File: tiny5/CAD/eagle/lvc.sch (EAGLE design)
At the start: 35 parts, among them J1 3,5MM_1X2_SCREWTERM, J2 3,5MM_1X2_SCREWTERM, J3 2X3_50MIL, Q1 FDC6312P, Q2 PMGD280UN, Q3 DMP3010LPS, Q4 DMP3010LPS, U1 LT3007, U2 ATTINY5, U3 LT1494

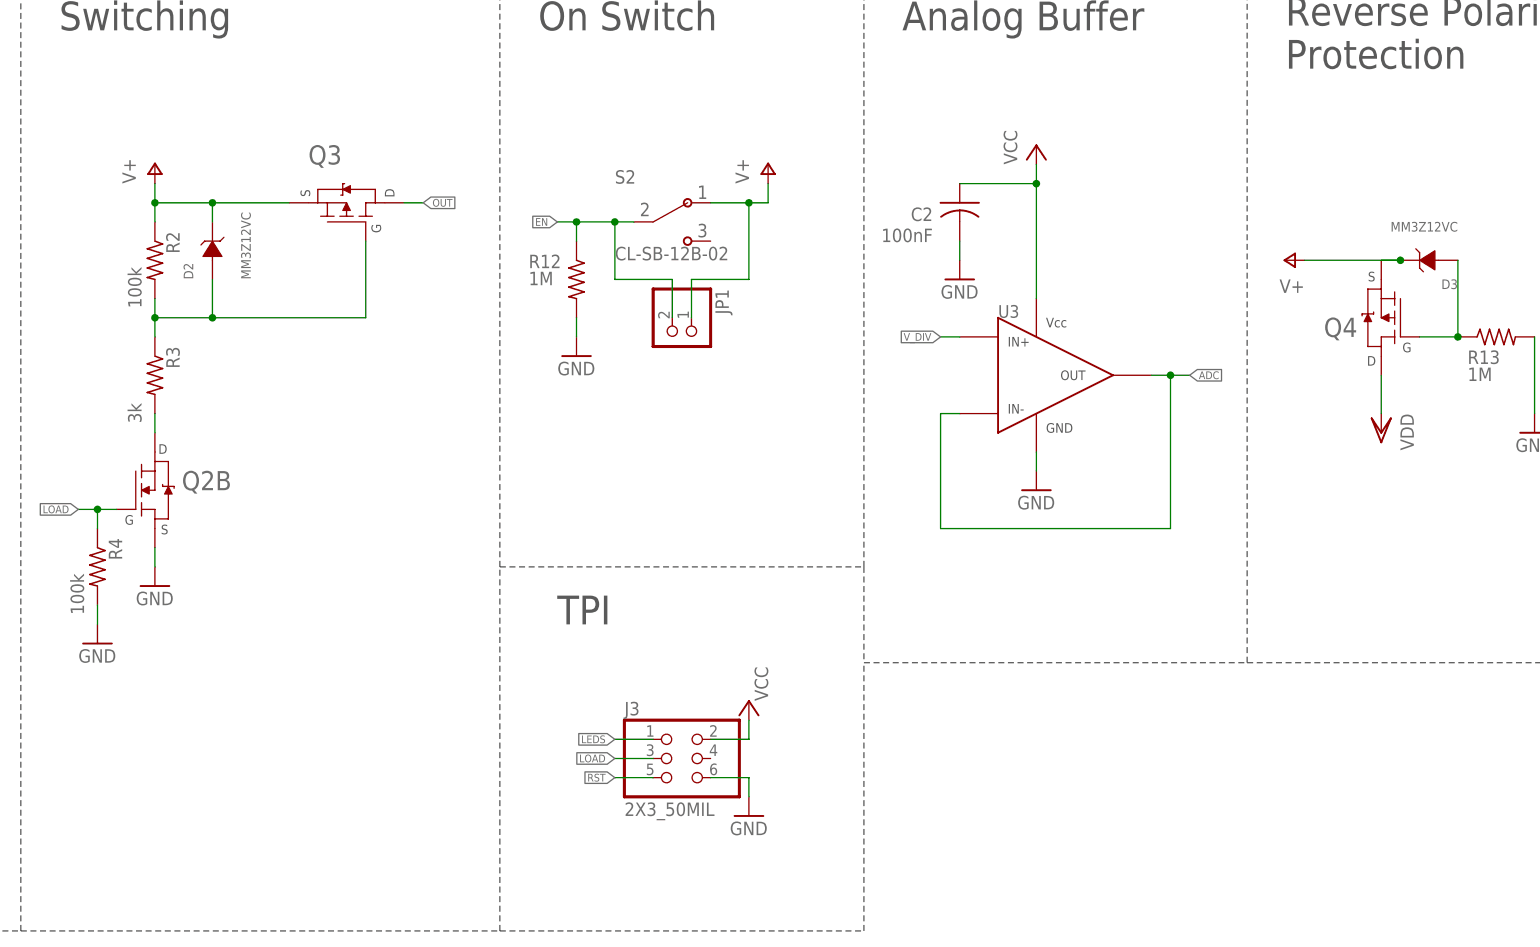
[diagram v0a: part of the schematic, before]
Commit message: yet another transistor (P-FET) update
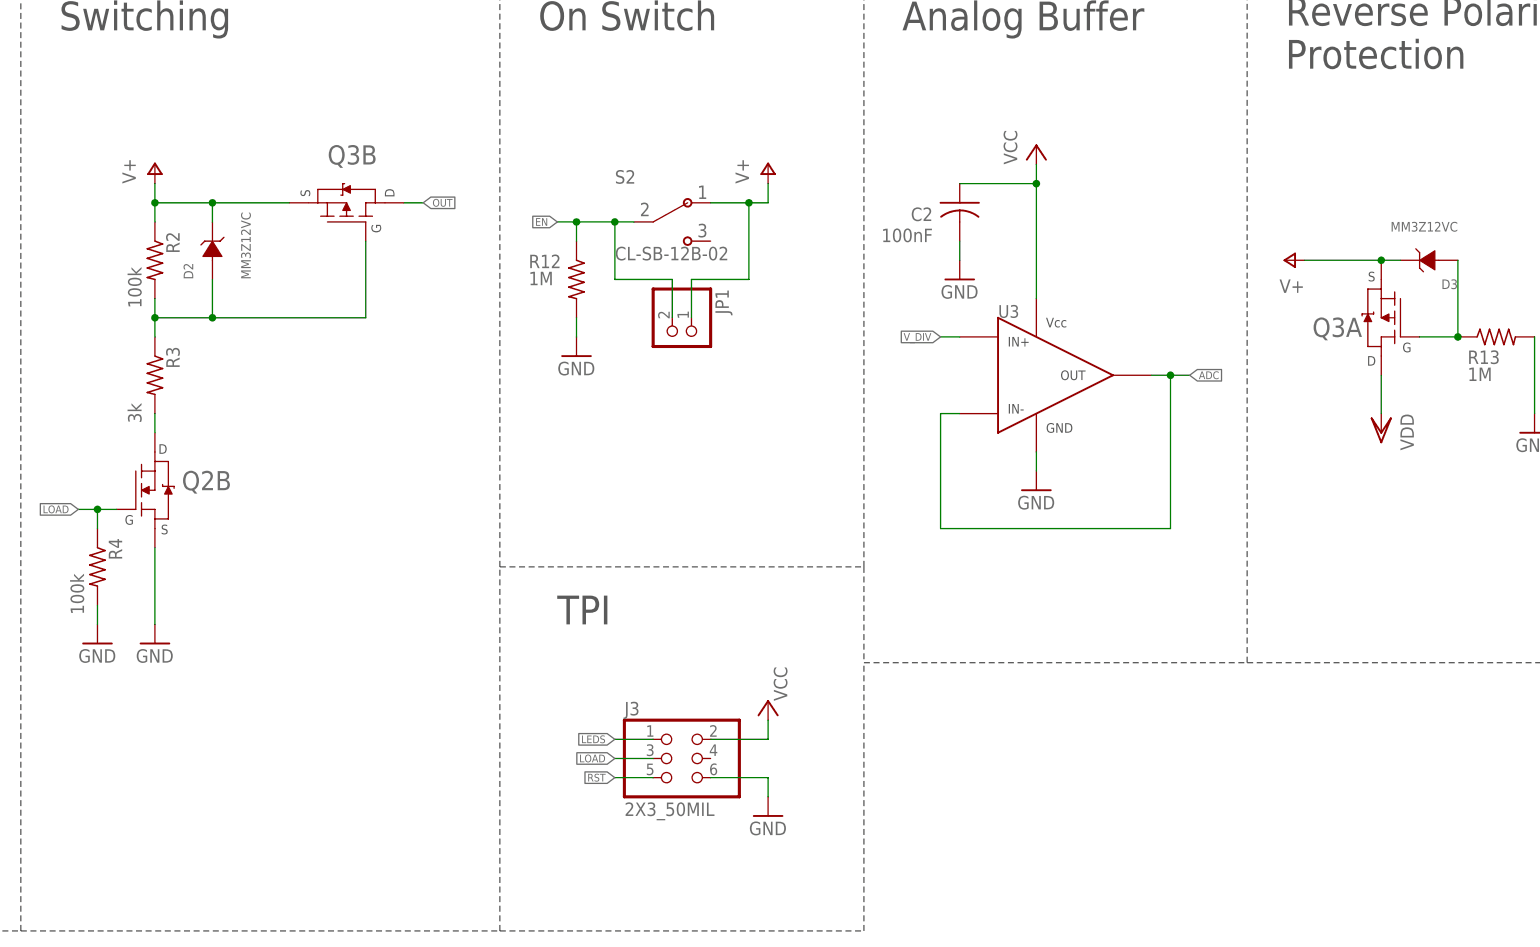
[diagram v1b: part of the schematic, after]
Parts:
- removed Q4: DMP3010LPS, AR_transistor:DMP3010LPS
- Q3: value DMP3010LPS -> SI7997DP; device AR_transistor:DMP3010LPS -> AR_transistor:SI7997DP
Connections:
- net N$5: now also Q3B.G; no longer Q3.G
- net N$6: now also Q3A.G; no longer Q4.G
- net OUT: now also Q3B.D; no longer Q3.D
- net V+: now also Q3A.S, Q3B.S; no longer Q3.S, Q4.S
- net VDD: now also Q3A.D; no longer Q4.D
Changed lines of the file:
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@@
 <part name="S2" library="AR_switches" deviceset="CL-SB-12B-02" device=""/>
 <part name="JP1" library="pinhead" deviceset="PINHD-1X2" device=""/>
-<part name="Q4" library="AR_transistor" deviceset="DMP3010LPS" device=""/>
 <part name="P+13" library="supply1" deviceset="V+" device=""/>
 <part name="VDD1" library="supply1" deviceset="VDD" device=""/>
@@
 <part name="R13" library="resistor" deviceset="R-US_" device="R0603" value="1M"/>
 <part name="GND19" library="supply1" deviceset="GND" device=""/>
-<part name="Q3" library="AR_transistor" deviceset="DMP3010LPS" device=""/>
+<part name="Q3" library="AR_transistor" deviceset="SI7997DP" device=""/>
 </parts>
 <sheets>
@@
 <instance part="D2" gate="G$1" x="83.82" y="96.52" rot="R90"/>
 <instance part="R3" gate="G$1" x="76.2" y="78.74" rot="R270"/>
-<instance part="GND7" gate="1" x="76.2" y="50.8"/>
+<instance part="GND7" gate="1" x="76.2" y="43.18"/>
 <instance part="GND8" gate="1" x="68.58" y="43.18"/>
 <instance part="R4" gate="G$1" x="68.58" y="53.34" rot="R270"/>
@@
 <instance part="TP1" gate="G$1" x="160.02" y="182.88"/>
 <instance part="J3" gate="G$1" x="147.32" y="27.94"/>
-<instance part="P+11" gate="VCC" x="154.94" y="35.56" smashed="yes">
-<attribute name="VALUE" x="157.48" y="35.56" size="1.778" layer="96" rot="R90"/>
-</instance>
-<instance part="GND17" gate="1" x="154.94" y="20.32"/>
+<instance part="P+11" gate="VCC" x="157.48" y="35.56" smashed="yes">
+<attribute name="VALUE" x="160.02" y="35.56" size="1.778" layer="96" rot="R90"/>
+</instance>
+<instance part="GND17" gate="1" x="157.48" y="20.32"/>
 <instance part="R12" gate="G$1" x="132.08" y="91.44" smashed="yes" rot="R270">
 <attribute name="NAME" x="125.73" y="92.9386" size="1.778" layer="95"/>
@@
 <instance part="S2" gate="G$1" x="144.78" y="99.06"/>
 <instance part="JP1" gate="G$1" x="144.78" y="83.82" rot="R270"/>
-<instance part="Q4" gate="G$1" x="238.76" y="86.36" smashed="yes">
-<attribute name="NAME" x="231.14" y="86.36" size="2.54" layer="95" rot="MR180"/>
-</instance>
 <instance part="P+13" gate="1" x="226.06" y="93.98" rot="R90"/>
 <instance part="VDD1" gate="G$1" x="251.46" y="157.48" rot="R270"/>
@@
 </instance>
 <instance part="GND19" gate="1" x="259.08" y="71.12"/>
-<instance part="Q3" gate="G$1" x="101.6" y="101.6" smashed="yes" rot="MR270">
-<attribute name="NAME" x="96.52" y="106.68" size="2.54" layer="95"/>
+<instance part="Q3" gate="B" x="101.6" y="101.6" smashed="yes" rot="MR270">
+<attribute name="NAME" x="99.06" y="106.68" size="2.54" layer="95"/>
+</instance>
+<instance part="Q3" gate="A" x="238.76" y="86.36" smashed="yes">
+<attribute name="NAME" x="236.22" y="83.82" size="2.54" layer="95" rot="MR0"/>
 </instance>
 </instances>
@@
 <pinref part="Q2" gate="B" pin="S"/>
 <pinref part="GND7" gate="1" pin="GND"/>
-<wire x1="76.2" y1="55.88" x2="76.2" y2="53.34" width="0.1524" layer="91"/>
+<wire x1="76.2" y1="55.88" x2="76.2" y2="45.72" width="0.1524" layer="91"/>
 </segment>
 <segment>
@@
 <segment>
 <pinref part="J3" gate="G$1" pin="6"/>
-<wire x1="149.86" y1="25.4" x2="154.94" y2="25.4" width="0.1524" layer="91"/>
-<wire x1="154.94" y1="25.4" x2="154.94" y2="22.86" width="0.1524" layer="91"/>
+<wire x1="149.86" y1="25.4" x2="157.48" y2="25.4" width="0.1524" layer="91"/>
+<wire x1="157.48" y1="25.4" x2="157.48" y2="22.86" width="0.1524" layer="91"/>
 <pinref part="GND17" gate="1" pin="GND"/>
 </segment>
@@
 <wire x1="83.82" y1="99.06" x2="83.82" y2="101.6" width="0.1524" layer="91"/>
 <junction x="83.82" y="101.6"/>
-<pinref part="Q3" gate="G$1" pin="S"/>
+<pinref part="Q3" gate="B" pin="S"/>
 </segment>
 <segment>
@@
 </segment>
 <segment>
-<pinref part="Q4" gate="G$1" pin="S"/>
 <pinref part="P+13" gate="1" pin="V+"/>
-<wire x1="228.6" y1="93.98" x2="241.3" y2="93.98" width="0.1524" layer="91"/>
+<wire x1="228.6" y1="93.98" x2="238.76" y2="93.98" width="0.1524" layer="91"/>
 <pinref part="D3" gate="G$1" pin="C"/>
-<junction x="241.3" y="93.98"/>
-<wire x1="241.3" y1="93.98" x2="238.76" y2="93.98" width="0.1524" layer="91"/>
+<pinref part="Q3" gate="A" pin="S"/>
+<wire x1="238.76" y1="93.98" x2="241.3" y2="93.98" width="0.1524" layer="91"/>
+<junction x="238.76" y="93.98"/>
 </segment>
 </net>
@@
 <pinref part="J3" gate="G$1" pin="2"/>
 <pinref part="P+11" gate="VCC" pin="VCC"/>
-<wire x1="149.86" y1="30.48" x2="154.94" y2="30.48" width="0.1524" layer="91"/>
-<wire x1="154.94" y1="30.48" x2="154.94" y2="33.02" width="0.1524" layer="91"/>
+<wire x1="149.86" y1="30.48" x2="157.48" y2="30.48" width="0.1524" layer="91"/>
+<wire x1="157.48" y1="30.48" x2="157.48" y2="33.02" width="0.1524" layer="91"/>
 </segment>
 </net>
@@
 <wire x1="76.2" y1="83.82" x2="76.2" y2="86.36" width="0.1524" layer="91"/>
 <junction x="76.2" y="86.36"/>
-<pinref part="Q3" gate="G$1" pin="G"/>
+<pinref part="Q3" gate="B" pin="G"/>
 </segment>
 </net>
@@
 <wire x1="109.22" y1="101.6" x2="111.76" y2="101.6" width="0.1524" layer="91"/>
 <label x="111.76" y="101.6" size="1.016" layer="95" xref="yes"/>
-<pinref part="Q3" gate="G$1" pin="D"/>
+<pinref part="Q3" gate="B" pin="D"/>
 </segment>
 <segment>
@@
 </segment>
 <segment>
-<pinref part="Q4" gate="G$1" pin="D"/>
 <pinref part="VDD2" gate="G$1" pin="VDD"/>
 <wire x1="238.76" y1="73.66" x2="238.76" y2="78.74" width="0.1524" layer="91"/>
+<pinref part="Q3" gate="A" pin="D"/>
 </segment>
 </net>
@@
 <pinref part="D3" gate="G$1" pin="A"/>
 <wire x1="248.92" y1="93.98" x2="248.92" y2="83.82" width="0.1524" layer="91"/>
-<pinref part="Q4" gate="G$1" pin="G"/>
 <wire x1="248.92" y1="83.82" x2="243.84" y2="83.82" width="0.1524" layer="91"/>
 <pinref part="R13" gate="G$1" pin="1"/>
 <junction x="248.92" y="83.82"/>
-</segment>
-</net>
+<pinref part="Q3" gate="A" pin="G"/>
+</segment>
+</net>

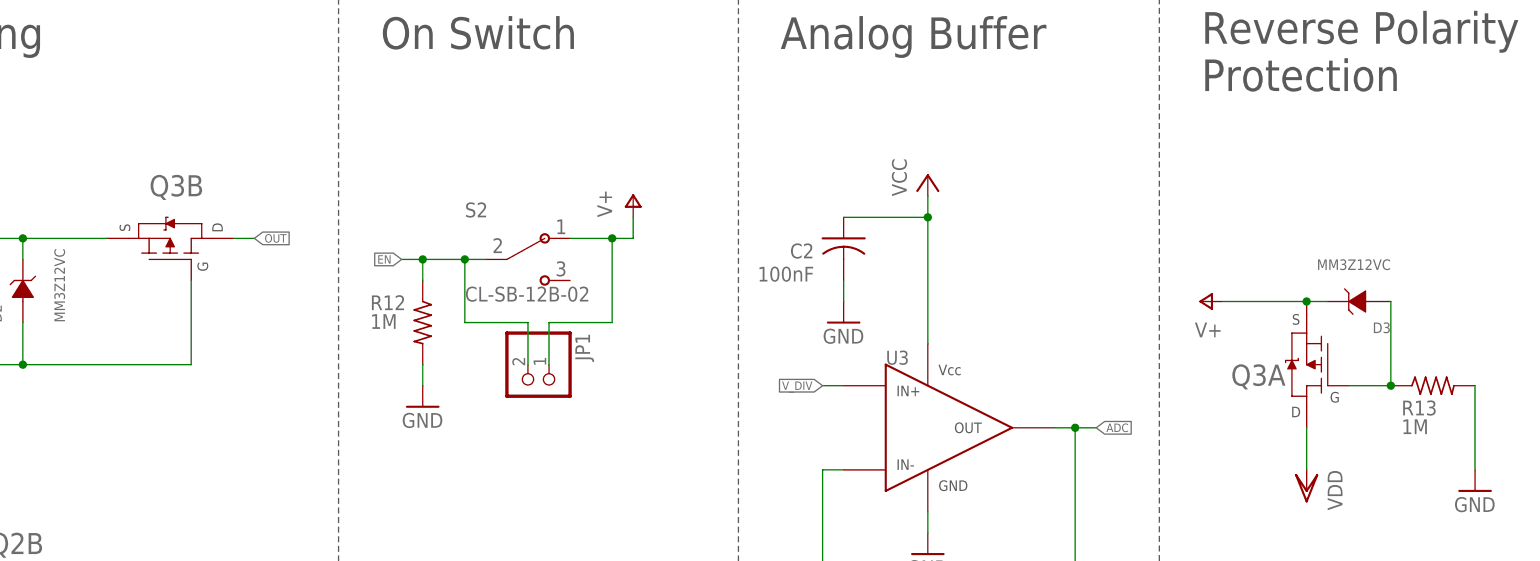
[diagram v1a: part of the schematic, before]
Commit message: Routed new transistor. Cleaned up transistor package definition
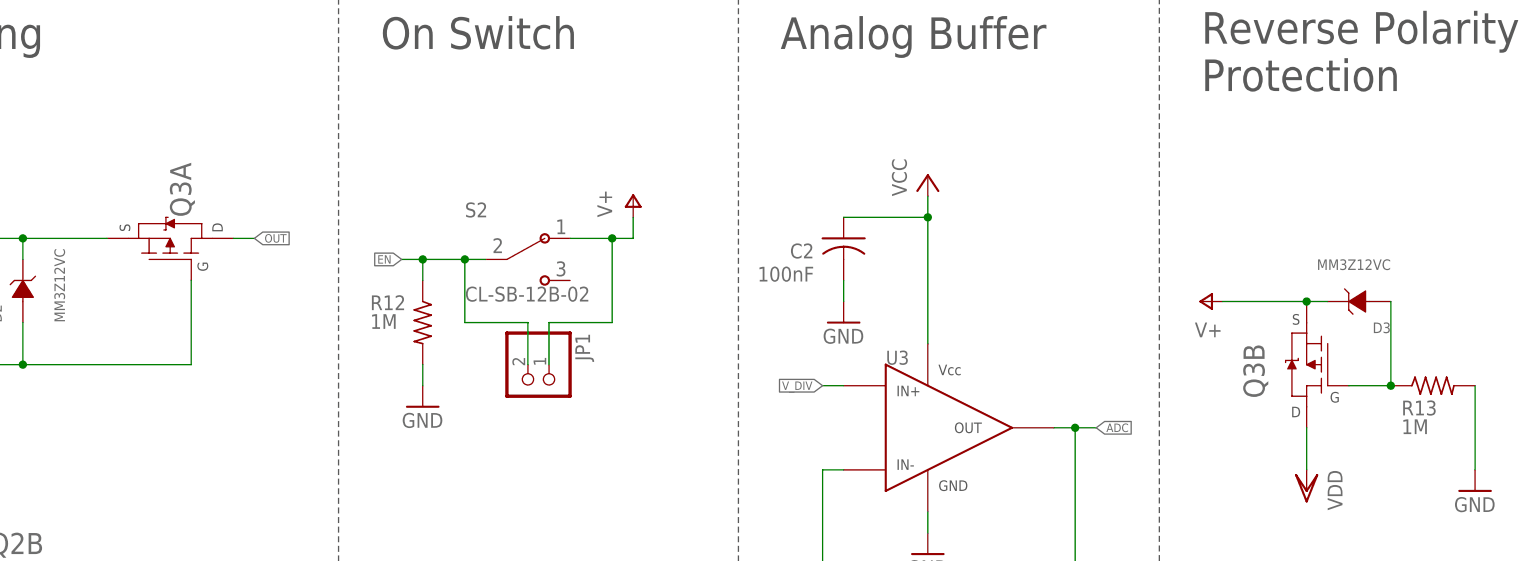
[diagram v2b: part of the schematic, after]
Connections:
- net N$5: now also Q3A.G; no longer Q3B.G
- net N$6: now also Q3B.G; no longer Q3A.G
- net OUT: now also Q3A.D; no longer Q3B.D
- net VDD: now also Q3B.D; no longer Q3A.D
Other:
- moved on the sheet: Q3A, Q3B
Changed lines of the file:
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@@
 <?xml version="1.0" encoding="utf-8"?>
 <!DOCTYPE eagle SYSTEM "eagle.dtd">
-<eagle version="7.6.0">
+<eagle version="6.5.0">
 <drawing>
 <settings>
@@
 </instance>
 <instance part="GND19" gate="1" x="259.08" y="71.12"/>
-<instance part="Q3" gate="B" x="101.6" y="101.6" smashed="yes" rot="MR270">
-<attribute name="NAME" x="99.06" y="106.68" size="2.54" layer="95"/>
-</instance>
-<instance part="Q3" gate="A" x="238.76" y="86.36" smashed="yes">
-<attribute name="NAME" x="236.22" y="83.82" size="2.54" layer="95" rot="MR0"/>
+<instance part="Q3" gate="B" x="238.76" y="86.36" smashed="yes">
+<attribute name="NAME" x="233.68" y="88.9" size="2.54" layer="95" rot="MR270"/>
+</instance>
+<instance part="Q3" gate="A" x="101.6" y="101.6" smashed="yes" rot="MR270">
+<attribute name="NAME" x="104.14" y="104.14" size="2.54" layer="95" rot="R90"/>
 </instance>
 </instances>
@@
 <segment>
 <pinref part="P+4" gate="1" pin="V+"/>
-<wire x1="93.98" y1="101.6" x2="83.82" y2="101.6" width="0.1524" layer="91"/>
 <wire x1="83.82" y1="101.6" x2="76.2" y2="101.6" width="0.1524" layer="91"/>
 <wire x1="76.2" y1="101.6" x2="76.2" y2="104.14" width="0.1524" layer="91"/>
@@
 <pinref part="D2" gate="G$1" pin="C"/>
 <wire x1="83.82" y1="99.06" x2="83.82" y2="101.6" width="0.1524" layer="91"/>
+<pinref part="Q3" gate="A" pin="S"/>
+<wire x1="93.98" y1="101.6" x2="83.82" y2="101.6" width="0.1524" layer="91"/>
 <junction x="83.82" y="101.6"/>
-<pinref part="Q3" gate="B" pin="S"/>
 </segment>
 <segment>
@@
 </segment>
 <segment>
+<pinref part="D3" gate="G$1" pin="C"/>
+<pinref part="Q3" gate="B" pin="S"/>
+<wire x1="241.3" y1="93.98" x2="238.76" y2="93.98" width="0.1524" layer="91"/>
 <pinref part="P+13" gate="1" pin="V+"/>
-<wire x1="228.6" y1="93.98" x2="238.76" y2="93.98" width="0.1524" layer="91"/>
-<pinref part="D3" gate="G$1" pin="C"/>
-<pinref part="Q3" gate="A" pin="S"/>
-<wire x1="238.76" y1="93.98" x2="241.3" y2="93.98" width="0.1524" layer="91"/>
+<wire x1="238.76" y1="93.98" x2="228.6" y2="93.98" width="0.1524" layer="91"/>
 <junction x="238.76" y="93.98"/>
 </segment>
@@
 <wire x1="76.2" y1="86.36" x2="83.82" y2="86.36" width="0.1524" layer="91"/>
 <wire x1="83.82" y1="86.36" x2="104.14" y2="86.36" width="0.1524" layer="91"/>
-<wire x1="104.14" y1="86.36" x2="104.14" y2="96.52" width="0.1524" layer="91"/>
 <pinref part="D2" gate="G$1" pin="A"/>
 <wire x1="83.82" y1="91.44" x2="83.82" y2="86.36" width="0.1524" layer="91"/>
@@
 <wire x1="76.2" y1="83.82" x2="76.2" y2="86.36" width="0.1524" layer="91"/>
 <junction x="76.2" y="86.36"/>
-<pinref part="Q3" gate="B" pin="G"/>
+<pinref part="Q3" gate="A" pin="G"/>
+<wire x1="104.14" y1="96.52" x2="104.14" y2="86.36" width="0.1524" layer="91"/>
 </segment>
 </net>
@@
 <net name="OUT" class="0">
 <segment>
-<wire x1="109.22" y1="101.6" x2="111.76" y2="101.6" width="0.1524" layer="91"/>
 <label x="111.76" y="101.6" size="1.016" layer="95" xref="yes"/>
-<pinref part="Q3" gate="B" pin="D"/>
+<pinref part="Q3" gate="A" pin="D"/>
+<wire x1="111.76" y1="101.6" x2="109.22" y2="101.6" width="0.1524" layer="91"/>
 </segment>
 <segment>
@@
 <segment>
 <pinref part="VDD2" gate="G$1" pin="VDD"/>
+<pinref part="Q3" gate="B" pin="D"/>
 <wire x1="238.76" y1="73.66" x2="238.76" y2="78.74" width="0.1524" layer="91"/>
-<pinref part="Q3" gate="A" pin="D"/>
 </segment>
 </net>
@@
 <pinref part="D3" gate="G$1" pin="A"/>
 <wire x1="248.92" y1="93.98" x2="248.92" y2="83.82" width="0.1524" layer="91"/>
-<wire x1="248.92" y1="83.82" x2="243.84" y2="83.82" width="0.1524" layer="91"/>
 <pinref part="R13" gate="G$1" pin="1"/>
+<pinref part="Q3" gate="B" pin="G"/>
+<wire x1="243.84" y1="83.82" x2="248.92" y2="83.82" width="0.1524" layer="91"/>
 <junction x="248.92" y="83.82"/>
-<pinref part="Q3" gate="A" pin="G"/>
-</segment>
-</net>
+</segment>
+</net>
